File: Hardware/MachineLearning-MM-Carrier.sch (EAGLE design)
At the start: 70 parts, among them J11 microSD, J2 JTAG, J3 QWIIC_RIGHT_ANGLE, J4 MICROMOD-2222-C, J5 SPI, J6 UART, J7 CAMERA-HIMAXFACEUP, J8 Dedicated, U3 AP2127K-1.8V, U4 LIS2DH12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

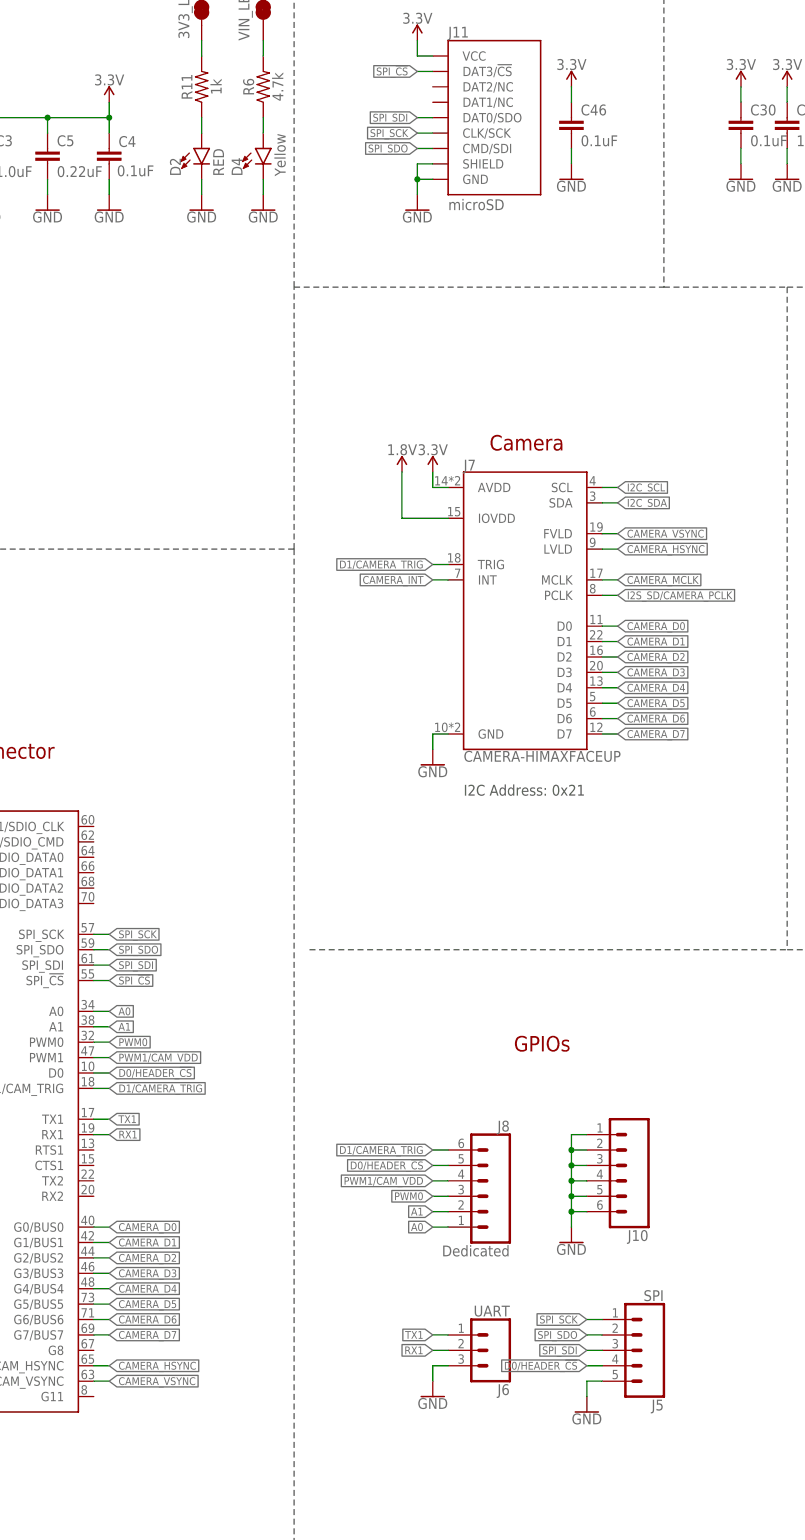
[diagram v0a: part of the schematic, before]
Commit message: Rename SPI lines for clarification
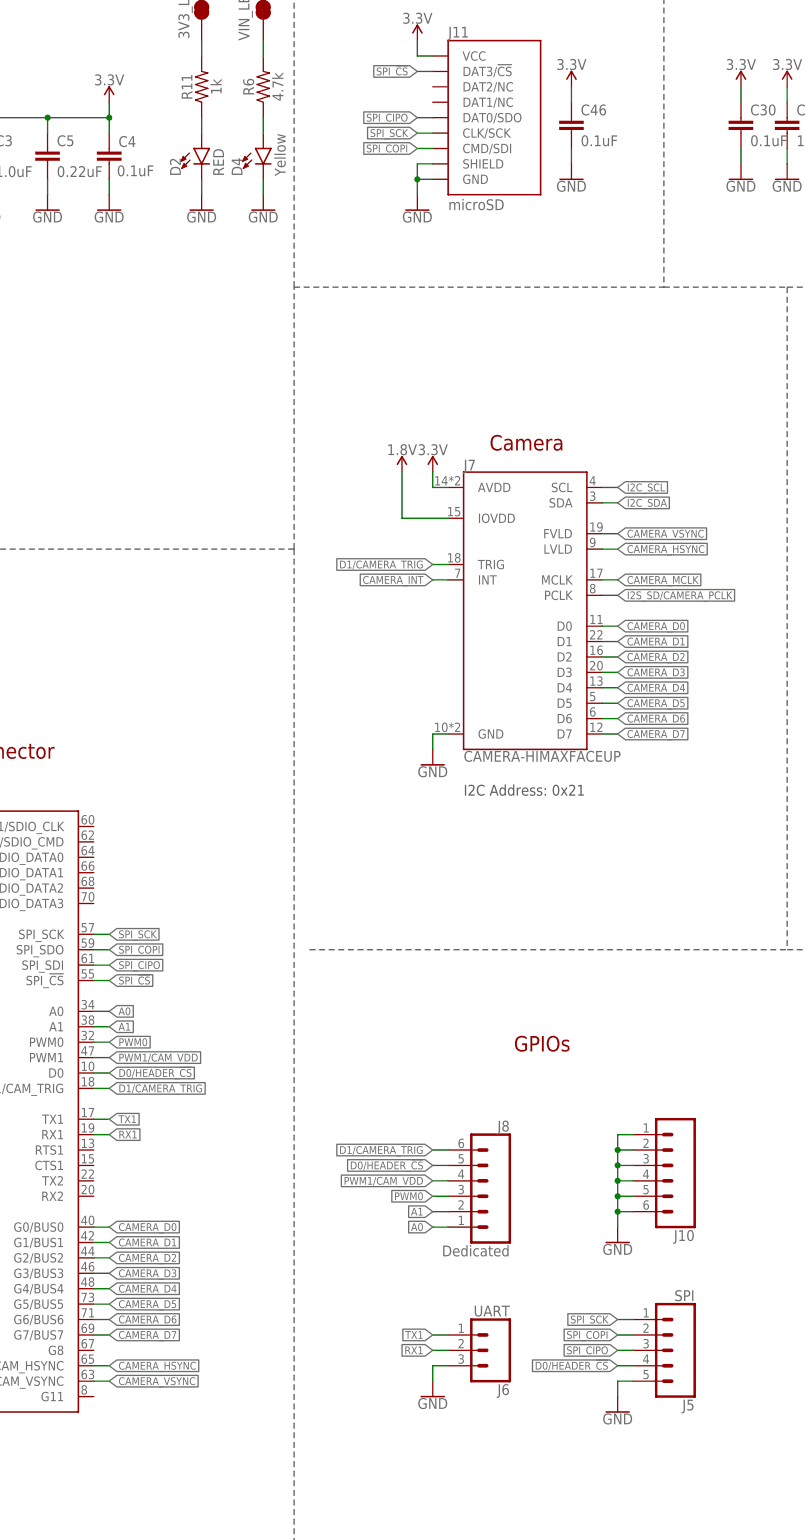
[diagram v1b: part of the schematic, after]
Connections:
- net SPI_SDI renamed SPI_CIPO
- net SPI_SDO renamed SPI_COPI
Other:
- moved on the sheet: J10, J5
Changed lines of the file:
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@@
 <attribute name="VALUE" x="342.9" y="251.46" size="1.778" layer="96" font="vector" rot="R90" align="top-left"/>
 </instance>
-<instance part="J5" gate="G$1" x="226.06" y="40.64" smashed="yes" rot="R180">
-<attribute name="VALUE" x="228.6" y="50.546" size="1.778" layer="96" font="vector" rot="R180"/>
-<attribute name="NAME" x="228.6" y="32.512" size="1.778" layer="95" font="vector" rot="R180"/>
+<instance part="J5" gate="G$1" x="231.14" y="40.64" smashed="yes" rot="R180">
+<attribute name="VALUE" x="233.68" y="50.546" size="1.778" layer="96" font="vector" rot="R180"/>
+<attribute name="NAME" x="233.68" y="32.512" size="1.778" layer="95" font="vector" rot="R180"/>
 </instance>
 <instance part="J8" gate="G$1" x="198.12" y="66.04" smashed="yes" rot="MR0">
@@
 <attribute name="NAME" x="203.2" y="76.708" size="1.778" layer="95" font="vector" rot="MR0"/>
 </instance>
-<instance part="J10" gate="G$1" x="220.98" y="71.12" smashed="yes" rot="R180">
-<attribute name="VALUE" x="226.06" y="81.026" size="1.778" layer="96" font="vector" rot="R180"/>
-<attribute name="NAME" x="226.06" y="60.452" size="1.778" layer="95" font="vector" rot="R180"/>
-</instance>
-<instance part="GND13" gate="1" x="213.36" y="58.42" smashed="yes">
-<attribute name="VALUE" x="213.36" y="58.166" size="1.778" layer="96" align="top-center"/>
-</instance>
-<instance part="GND14" gate="1" x="215.9" y="30.48" smashed="yes">
-<attribute name="VALUE" x="215.9" y="30.226" size="1.778" layer="96" align="top-center"/>
+<instance part="J10" gate="G$1" x="228.6" y="71.12" smashed="yes" rot="R180">
+<attribute name="VALUE" x="233.68" y="81.026" size="1.778" layer="96" font="vector" rot="R180"/>
+<attribute name="NAME" x="233.68" y="60.452" size="1.778" layer="95" font="vector" rot="R180"/>
+</instance>
+<instance part="GND13" gate="1" x="220.98" y="58.42" smashed="yes">
+<attribute name="VALUE" x="220.98" y="58.166" size="1.778" layer="96" align="top-center"/>
+</instance>
+<instance part="GND14" gate="1" x="220.98" y="30.48" smashed="yes">
+<attribute name="VALUE" x="220.98" y="30.226" size="1.778" layer="96" align="top-center"/>
 </instance>
 <instance part="LOGO2" gate="G$1" x="360.68" y="40.64" smashed="yes"/>
@@
 </busses>
 <nets>
-<net name="SPI_SDI" class="0">
+<net name="SPI_CIPO" class="0">
 <segment>
 <wire x1="190.5" y1="243.84" x2="187.96" y2="243.84" width="0.1524" layer="91"/>
@@
 <segment>
 <pinref part="J5" gate="G$1" pin="3"/>
-<wire x1="218.44" y1="40.64" x2="215.9" y2="40.64" width="0.1524" layer="91"/>
-<label x="215.9" y="40.64" size="1.27" layer="95" rot="R180" xref="yes"/>
+<wire x1="223.52" y1="40.64" x2="220.98" y2="40.64" width="0.1524" layer="91"/>
+<label x="220.98" y="40.64" size="1.27" layer="95" rot="R180" xref="yes"/>
 </segment>
 <segment>
@@
 <segment>
 <pinref part="J5" gate="G$1" pin="1"/>
-<wire x1="218.44" y1="45.72" x2="215.9" y2="45.72" width="0.1524" layer="91"/>
-<label x="215.9" y="45.72" size="1.27" layer="95" rot="R180" xref="yes"/>
+<wire x1="223.52" y1="45.72" x2="220.98" y2="45.72" width="0.1524" layer="91"/>
+<label x="220.98" y="45.72" size="1.27" layer="95" rot="R180" xref="yes"/>
 </segment>
 <segment>
@@
 </segment>
 </net>
-<net name="SPI_SDO" class="0">
+<net name="SPI_COPI" class="0">
 <segment>
 <wire x1="190.5" y1="238.76" x2="187.96" y2="238.76" width="0.1524" layer="91"/>
@@
 <segment>
 <pinref part="J5" gate="G$1" pin="2"/>
-<wire x1="218.44" y1="43.18" x2="215.9" y2="43.18" width="0.1524" layer="91"/>
-<label x="215.9" y="43.18" size="1.27" layer="95" rot="R180" xref="yes"/>
+<wire x1="223.52" y1="43.18" x2="220.98" y2="43.18" width="0.1524" layer="91"/>
+<label x="220.98" y="43.18" size="1.27" layer="95" rot="R180" xref="yes"/>
 </segment>
 <segment>
@@
 <segment>
 <pinref part="J10" gate="G$1" pin="1"/>
-<wire x1="215.9" y1="76.2" x2="213.36" y2="76.2" width="0.1524" layer="91"/>
-<wire x1="213.36" y1="76.2" x2="213.36" y2="73.66" width="0.1524" layer="91"/>
+<wire x1="223.52" y1="76.2" x2="220.98" y2="76.2" width="0.1524" layer="91"/>
+<wire x1="220.98" y1="76.2" x2="220.98" y2="73.66" width="0.1524" layer="91"/>
 <pinref part="J10" gate="G$1" pin="6"/>
-<wire x1="213.36" y1="73.66" x2="213.36" y2="71.12" width="0.1524" layer="91"/>
-<wire x1="213.36" y1="71.12" x2="213.36" y2="68.58" width="0.1524" layer="91"/>
-<wire x1="213.36" y1="68.58" x2="213.36" y2="66.04" width="0.1524" layer="91"/>
-<wire x1="213.36" y1="66.04" x2="213.36" y2="63.5" width="0.1524" layer="91"/>
-<wire x1="213.36" y1="63.5" x2="213.36" y2="60.96" width="0.1524" layer="91"/>
-<wire x1="215.9" y1="63.5" x2="213.36" y2="63.5" width="0.1524" layer="91"/>
-<junction x="213.36" y="63.5"/>
+<wire x1="220.98" y1="73.66" x2="220.98" y2="71.12" width="0.1524" layer="91"/>
+<wire x1="220.98" y1="71.12" x2="220.98" y2="68.58" width="0.1524" layer="91"/>
+<wire x1="220.98" y1="68.58" x2="220.98" y2="66.04" width="0.1524" layer="91"/>
+<wire x1="220.98" y1="66.04" x2="220.98" y2="63.5" width="0.1524" layer="91"/>
+<wire x1="220.98" y1="63.5" x2="220.98" y2="60.96" width="0.1524" layer="91"/>
+<wire x1="223.52" y1="63.5" x2="220.98" y2="63.5" width="0.1524" layer="91"/>
+<junction x="220.98" y="63.5"/>
 <pinref part="J10" gate="G$1" pin="5"/>
-<wire x1="215.9" y1="66.04" x2="213.36" y2="66.04" width="0.1524" layer="91"/>
-<junction x="213.36" y="66.04"/>
+<wire x1="223.52" y1="66.04" x2="220.98" y2="66.04" width="0.1524" layer="91"/>
+<junction x="220.98" y="66.04"/>
 <pinref part="J10" gate="G$1" pin="4"/>
-<wire x1="215.9" y1="68.58" x2="213.36" y2="68.58" width="0.1524" layer="91"/>
-<junction x="213.36" y="68.58"/>
+<wire x1="223.52" y1="68.58" x2="220.98" y2="68.58" width="0.1524" layer="91"/>
+<junction x="220.98" y="68.58"/>
 <pinref part="J10" gate="G$1" pin="3"/>
-<wire x1="215.9" y1="71.12" x2="213.36" y2="71.12" width="0.1524" layer="91"/>
-<junction x="213.36" y="71.12"/>
+<wire x1="223.52" y1="71.12" x2="220.98" y2="71.12" width="0.1524" layer="91"/>
+<junction x="220.98" y="71.12"/>
 <pinref part="J10" gate="G$1" pin="2"/>
-<wire x1="215.9" y1="73.66" x2="213.36" y2="73.66" width="0.1524" layer="91"/>
-<junction x="213.36" y="73.66"/>
+<wire x1="223.52" y1="73.66" x2="220.98" y2="73.66" width="0.1524" layer="91"/>
+<junction x="220.98" y="73.66"/>
 <pinref part="GND13" gate="1" pin="GND"/>
 </segment>
 <segment>
 <pinref part="J5" gate="G$1" pin="5"/>
-<wire x1="218.44" y1="35.56" x2="215.9" y2="35.56" width="0.1524" layer="91"/>
-<wire x1="215.9" y1="35.56" x2="215.9" y2="33.02" width="0.1524" layer="91"/>
+<wire x1="223.52" y1="35.56" x2="220.98" y2="35.56" width="0.1524" layer="91"/>
+<wire x1="220.98" y1="35.56" x2="220.98" y2="33.02" width="0.1524" layer="91"/>
 <pinref part="GND14" gate="1" pin="GND"/>
 </segment>
@@
 <segment>
 <pinref part="J5" gate="G$1" pin="4"/>
-<wire x1="218.44" y1="38.1" x2="215.9" y2="38.1" width="0.1524" layer="91"/>
-<label x="215.9" y="38.1" size="1.27" layer="95" rot="R180" xref="yes"/>
-</segment>
-<segment>
+<wire x1="223.52" y1="38.1" x2="220.98" y2="38.1" width="0.1524" layer="91"/>
+<label x="220.98" y="38.1" size="1.27" layer="95" rot="R180" xref="yes"/>
+</segment>
+<segment>

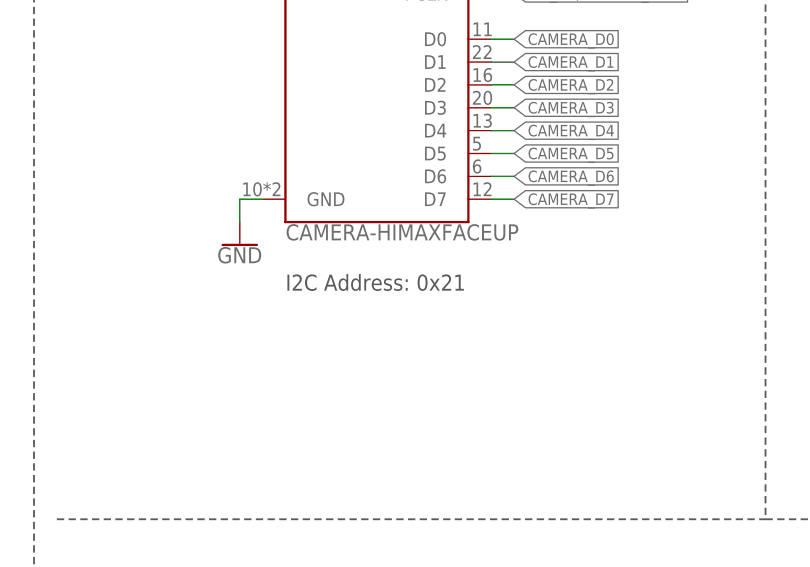
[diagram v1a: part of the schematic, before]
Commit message: Update schematic with correct 0x24 camera I2C address
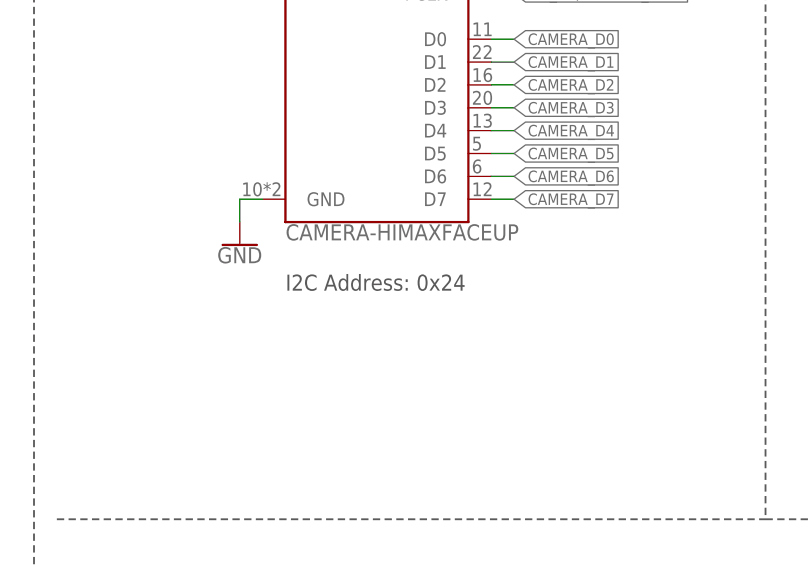
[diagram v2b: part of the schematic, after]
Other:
- note added: "I2C Address: 0x24"
- note removed: "I2C Address: 0x21"
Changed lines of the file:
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@@
 <?xml version="1.0" encoding="utf-8"?>
 <!DOCTYPE eagle SYSTEM "eagle.dtd">
-<eagle version="9.5.2">
+<eagle version="9.6.2">
 <drawing>
 <settings>
@@
 <text x="266.7" y="259.08" size="1.778" layer="97">I2C Address:
 0x19 (SA0 = 1)</text>
-<text x="195.58" y="132.08" size="1.778" layer="97">I2C Address: 0x21</text>
+<text x="195.58" y="132.08" size="1.778" layer="97">I2C Address: 0x24</text>
 <text x="198.12" y="266.7" size="2.54" layer="94" align="center">μSD</text>
 <text x="287.02" y="154.94" size="1.778" layer="97" rot="R90">300uA Leakage</text>
